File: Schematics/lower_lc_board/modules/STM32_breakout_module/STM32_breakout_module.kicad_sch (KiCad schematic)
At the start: 54 parts, among them J2 SWD_CONN, J3 USB_C_CONN, Q4 2N7002, SW1 SW_STM_RESET, SW2 SW_STM_BOOT_MODE, U5 STM32F103CBT6, U6 W25Q128JVS, U7 ISO1044BDR, U8 CP2102N-Axx-xQFN28, Y1 X322516MMB4SI

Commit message: organizational work
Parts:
- C45: JLCPCB (none) -> C49678
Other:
- moved on the sheet: C22, C45
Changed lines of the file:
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@@
 	)
 	(rectangle
-		(start 104.14 160.02)
-		(end 151.13 185.42)
+		(start 104.394 160.02)
+		(end 144.526 181.356)
 		(stroke
 			(width 0)
@@
 		)
 	)
-	(text "place near PA7 to filter switching noise from adjacent MCO pin "
+	(text "place near PA7 to \nfilter switching noise from \nadjacent MCO pin "
 		(exclude_from_sim no)
-		(at 131.318 179.07 0)
+		(at 154.94 185.166 0)
 		(effects
 			(font
@@
 	(global_label "TEMP_SENSE"
 		(shape input)
-		(at 109.22 170.18 270)
+		(at 149.86 177.8 90)
 		(fields_autoplaced yes)
 		(effects
@@
 		)
 		(property "Intersheetrefs" "${INTERSHEET_REFS}"
-			(at 109.22 185.0183 90)
+			(at 149.86 162.9617 90)
 			(effects
 				(font
@@
 		(lib_name "GND_2")
 		(lib_id "power:GND")
-		(at 116.84 170.18 90)
+		(at 160.02 170.18 180)
 		(unit 1)
 		(exclude_from_sim no)
@@
 		(dnp no)
 		(property "Reference" "#PWR070"
-			(at 123.19 170.18 0)
+			(at 160.02 163.83 0)
 			(effects
 				(font
@@
 		)
 		(property "Value" "GND"
-			(at 120.65 170.1799 90)
+			(at 160.0199 166.37 90)
 			(effects
 				(font
@@
 		)
 		(property "Footprint" ""
-			(at 116.84 170.18 0)
+			(at 160.02 170.18 0)
 			(effects
 				(font
@@
 		)
 		(property "Datasheet" ""
-			(at 116.84 170.18 0)
+			(at 160.02 170.18 0)
 			(effects
 				(font
@@
 		)
 		(property "Description" "Power symbol creates a global label with name \"GND\" , ground"
-			(at 116.84 170.18 0)
+			(at 160.02 170.18 0)
 			(effects
 				(font
@@
 	(symbol
 		(lib_id "Device:C")
-		(at 113.03 170.18 270)
+		(at 160.02 173.99 0)
 		(unit 1)
 		(exclude_from_sim no)
@@
 		(dnp no)
 		(property "Reference" "C45"
-			(at 113.03 164.338 90)
+			(at 154.686 164.338 0)
 			(effects
 				(font
@@
 		)
 		(property "Value" "0.1uF"
-			(at 113.03 166.878 90)
+			(at 154.686 166.878 0)
 			(effects
 				(font
@@
 		)
 		(property "Footprint" "Capacitor_SMD:C_0805_2012Metric"
-			(at 109.22 171.1452 0)
+			(at 160.9852 177.8 0)
 			(effects
 				(font
@@
 		)
 		(property "Datasheet" "~"
-			(at 113.03 170.18 0)
+			(at 160.02 173.99 0)
 			(effects
 				(font
@@
 		)
 		(property "Description" "Unpolarized capacitor"
-			(at 113.03 170.18 0)
+			(at 160.02 173.99 0)
+			(effects
+				(font
+					(size 1.27 1.27)
+				)
+				(hide yes)
+			)
+		)
+		(property "JLCPCB" "C49678"
+			(at 160.02 173.99 0)
 			(effects
 				(font
@@
 	(symbol
 		(lib_id "Device:C")
-		(at 201.93 140.97 90)
+		(at 198.12 147.32 0)
 		(unit 1)
 		(exclude_from_sim no)
@@
 		(on_board yes)
 		(dnp no)
+		(fields_autoplaced yes)
 		(property "Reference" "C22"
-			(at 203.454 135.128 90)
+			(at 201.93 146.0499 0)
 			(effects
 				(font
@@
 		)
 		(property "Value" "0.1uF"
-			(at 204.47 137.16 90)
+			(at 201.93 148.5899 0)
 			(effects
 				(font
@@
 		)
 		(property "Footprint" "Capacitor_SMD:C_0603_1608Metric"
-			(at 205.74 140.0048 0)
+			(at 199.0852 151.13 0)
 			(effects
 				(font
@@
 		)
 		(property "Datasheet" "~"
-			(at 201.93 140.97 0)
+			(at 198.12 147.32 0)
 			(effects
 				(font
@@
 		)
 		(property "Description" "Unpolarized capacitor"
-			(at 201.93 140.97 0)
+			(at 198.12 147.32 0)
 			(effects
 				(font
@@
 	(symbol
 		(lib_id "power:GND")
-		(at 205.74 140.97 0)
+		(at 198.12 151.13 270)
 		(unit 1)
 		(exclude_from_sim no)
@@
 		(dnp no)
 		(property "Reference" "#PWR056"
-			(at 205.74 147.32 0)
+			(at 191.77 151.13 0)
 			(effects
 				(font
@@
 		)
 		(property "Value" "GND"
-			(at 205.74 144.018 90)
+			(at 195.072 151.13 90)
 			(effects
 				(font
@@
 		)
 		(property "Footprint" ""
-			(at 205.74 140.97 0)
+			(at 198.12 151.13 0)
 			(effects
 				(font
@@
 		)
 		(property "Datasheet" ""
-			(at 205.74 140.97 0)
+			(at 198.12 151.13 0)
 			(effects
 				(font
@@
 		)
 		(property "Description" "Power symbol creates a global label with name \"GND\" , ground"
-			(at 205.74 140.97 0)
+			(at 198.12 151.13 0)
 			(effects
 				(font
@@
 	(symbol
 		(lib_id "power:+5V")
-		(at 198.12 140.97 180)
+		(at 198.12 143.51 90)
 		(unit 1)
 		(exclude_from_sim no)
@@
 		(fields_autoplaced yes)
 		(property "Reference" "#PWR053"
-			(at 198.12 137.16 0)
+			(at 201.93 143.51 0)
 			(effects
 				(font
@@
 		)
 		(property "Value" "+5V"
-			(at 198.1199 144.78 90)
+			(at 194.31 143.5099 90)
 			(effects
 				(font
@@
 		)
 		(property "Footprint" ""
-			(at 198.12 140.97 0)
+			(at 198.12 143.51 0)
 			(effects
 				(font
@@
 		)
 		(property "Datasheet" ""
-			(at 198.12 140.97 0)
+			(at 198.12 143.51 0)
 			(effects
 				(font
@@
 		)
 		(property "Description" "Power symbol creates a global label with name \"+5V\""
-			(at 198.12 140.97 0)
+			(at 198.12 143.51 0)
 			(effects
 				(font

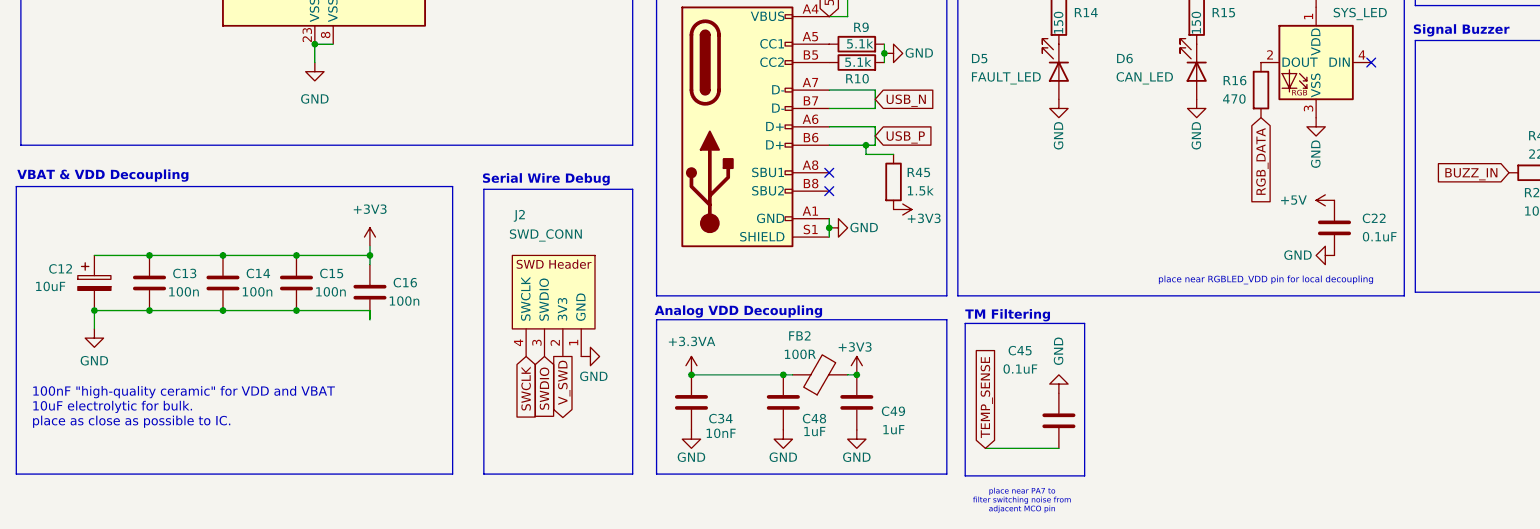
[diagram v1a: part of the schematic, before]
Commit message: more organizational work, add shared footprint, model, symbol dirs and clean up individuals
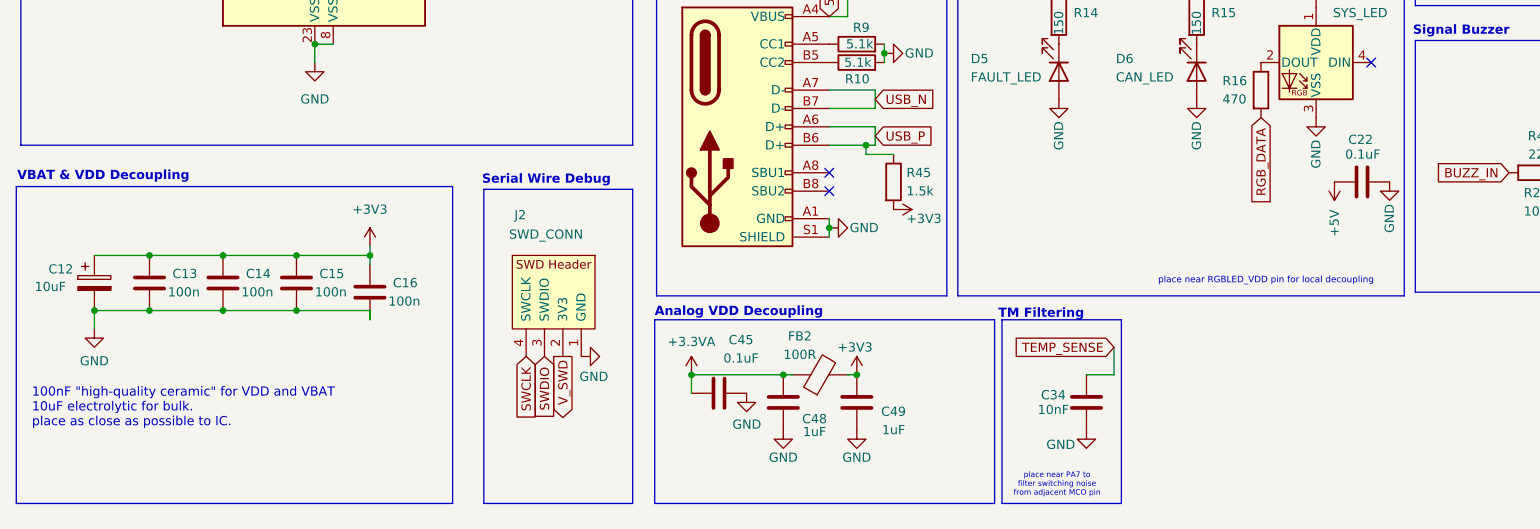
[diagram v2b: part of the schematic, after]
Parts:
- C45: JLCPCB C49678 -> (none)
- FB2: footprint BLM31KN121SN1L:BEADC3216X180N -> Resistor_SMD:R_0805_2012Metric
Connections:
- net +3.3VA: now also C45.2; no longer C34.2
- net TEMP_SENSE: now also C34.2; no longer C45.2
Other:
- title: (none) -> HYDRA | STM32 Breakout Circuitry
- moved on the sheet: C22, C34, C45

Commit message: routing work
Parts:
- removed U8: CP2102N-Axx-xQFN28, Package_DFN_QFN:QFN-28-1EP_5x5mm_P0.5mm_EP3.35x3.35mm, symbol Interface_USB:CP2102N-Axx-xQFN28
- added R48: 10k, Resistor_SMD:R_0402_1005Metric, symbol Device:R
- added U8: CP2102N-Axx-xQFN20, CP2102N_A02_GQFN20:QFN20_CP2102N_SIL, symbol Interface_USB:CP2102N-Axx-xQFN20
- C45: footprint Capacitor_SMD:C_0805_2012Metric -> Capacitor_SMD:C_0603_1608Metric; JLCPCB (none) -> C14663
- C48, C49: footprint Capacitor_SMD:C_0805_2012Metric -> Capacitor_SMD:C_0603_1608Metric; JLCPCB C28323 -> C15849
- R10, R9: footprint Resistor_SMD:R_0603_1608Metric -> Resistor_SMD:R_0402_1005Metric; JLCPCB (none) -> C25905
- R11: footprint Resistor_SMD:R_0603_1608Metric -> Resistor_SMD:R_0402_1005Metric; JLCPCB C31850 -> C25768
- R12: footprint Resistor_SMD:R_0603_1608Metric -> Resistor_SMD:R_0402_1005Metric; JLCPCB C25819 -> C25792
- R13: footprint Resistor_SMD:R_0603_1608Metric -> Capacitor_SMD:C_0402_1005Metric; JLCPCB C21190 -> C11702
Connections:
- net +3V3: now also R48.1, U8.6 (VDD), U8.7 (VREGIN)
- net FL_CS: now also R48.2
- net GND: now also U8.12 (GND), U8.21 (GND), U8.3 (GND)
- net USART_RX: now also U8.18 (TXD)
- net USART_TX: now also U8.17 (RXD)
- net USB_N: now also U8.5 (D-)
- net USB_P: now also U8.4 (D+)
- net at C20.2, R11.1, R12.2: now also U8.8 (VBUS)
- net at R13.1: now also U8.9 (~{RST})
- net ADC_MISO renamed SPI_MISO
- net SPI_MISO: now also U6.2 (DO(IO1))
- net ADC_MOSI renamed SPI_MOSI
- net SPI_MOSI: now also U6.5 (DI(IO0))
- net ADC_SCLK renamed SPI_SCLK
- net SPI_SCLK: now also U6.6 (CLK)
- net FL_MISO: no longer names the net of U5.27 (PB14)
- net FL_MISO: no longer U6.2 (DO(IO1))
- net FL_MOSI: no longer names the net of U5.28 (PB15)
- net FL_MOSI: no longer U6.5 (DI(IO0))
- net FL_SCK: no longer names the net of U5.26 (PB13)
- net FL_SCK: no longer U6.6 (CLK)
- no-connect marks 26 -> 17

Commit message: routing work
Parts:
- R12: now not fitted
- R14, R15: value 150 -> 220; footprint Resistor_SMD:R_0603_1608Metric -> Resistor_SMD:R_0402_1005Metric; JLCPCB (none) -> C25104
- R46: JLCPCB (none) -> C25104
- TP7, TP8: footprint TestPoint:TestPoint_Pad_1.0x1.0mm -> TestPoint:TestPoint_Pad_D1.0mm
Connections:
- net FAULT_LED: now also U5.29 (PA8); no longer U5.30 (PA9)
- net VALVE1_CTRL: now also U5.26 (PB13); no longer U5.31 (PA10)
- net VALVE2_CTRL: now also U5.27 (PB14); no longer U5.29 (PA8)
- new net VSOL-SW: U5.31 (PA10)
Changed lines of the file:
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@@
 		)
 	)
+	(global_label "FAULT_LED"
+		(shape input)
+		(at 74.93 68.58 0)
+		(fields_autoplaced yes)
+		(effects
+			(font
+				(size 1.27 1.27)
+			)
+			(justify left)
+		)
+		(property "Intersheetrefs" "${INTERSHEET_REFS}"
+			(at 87.8333 68.58 0)
+			(effects
+				(font
+					(size 1.27 1.27)
+				)
+				(justify left)
+				(hide yes)
+			)
+		)
+	)
 	(global_label "SWCLK"
 		(shape input)
@@
 		)
 	)
+	(global_label "VSOL-SW"
+		(shape input)
+		(at 74.93 73.66 0)
+		(fields_autoplaced yes)
+		(effects
+			(font
+				(size 1.27 1.27)
+			)
+			(justify left)
+		)
+		(property "Intersheetrefs" "${INTERSHEET_REFS}"
+			(at 86.8052 73.66 0)
+			(effects
+				(font
+					(size 1.27 1.27)
+				)
+				(justify left)
+				(hide yes)
+			)
+		)
+	)
 	(global_label "BOOT0"
 		(shape output)
@@
 		)
 	)
-	(global_label "VALVE1_CTRL"
-		(shape input)
-		(at 74.93 73.66 0)
-		(fields_autoplaced yes)
-		(effects
-			(font
-				(size 1.27 1.27)
-			)
-			(justify left)
-		)
-		(property "Intersheetrefs" "${INTERSHEET_REFS}"
-			(at 90.0709 73.66 0)
-			(effects
-				(font
-					(size 1.27 1.27)
-				)
-				(justify left)
-				(hide yes)
-			)
-		)
-	)
 	(global_label "BUZZ_IN"
 		(shape input)
@@
 		)
 	)
-	(global_label "FAULT_LED"
+	(global_label "VALVE2_CTRL"
 		(shape input)
-		(at 74.93 71.12 0)
+		(at 41.91 111.76 180)
 		(fields_autoplaced yes)
 		(effects
@@
 				(size 1.27 1.27)
 			)
-			(justify left)
+			(justify right)
 		)
 		(property "Intersheetrefs" "${INTERSHEET_REFS}"
-			(at 87.8333 71.12 0)
+			(at 26.7691 111.76 0)
 			(effects
 				(font
 					(size 1.27 1.27)
 				)
-				(justify left)
+				(justify right)
 				(hide yes)
 			)
@@
 		)
 	)
-	(global_label "VALVE2_CTRL"
-		(shape input)
-		(at 74.93 68.58 0)
-		(fields_autoplaced yes)
-		(effects
-			(font
-				(size 1.27 1.27)
-			)
-			(justify left)
-		)
-		(property "Intersheetrefs" "${INTERSHEET_REFS}"
-			(at 90.0709 68.58 0)
-			(effects
-				(font
-					(size 1.27 1.27)
-				)
-				(justify left)
-				(hide yes)
-			)
-		)
-	)
 	(global_label "RESET_FL"
 		(shape output)
@@
 		)
 	)
+	(global_label "VALVE1_CTRL"
+		(shape input)
+		(at 41.91 109.22 180)
+		(fields_autoplaced yes)
+		(effects
+			(font
+				(size 1.27 1.27)
+			)
+			(justify right)
+		)
+		(property "Intersheetrefs" "${INTERSHEET_REFS}"
+			(at 26.7691 109.22 0)
+			(effects
+				(font
+					(size 1.27 1.27)
+				)
+				(justify right)
+				(hide yes)
+			)
+		)
+	)
 	(symbol
 		(lib_id "Device:C_Polarized")
@@
 			)
 		)
+		(property "JLCPCB" "C25104"
+			(at 226.06 139.7 0)
+			(effects
+				(font
+					(size 1.27 1.27)
+				)
+				(hide yes)
+			)
+		)
 		(pin "2"
 		)
@@
 			)
 		)
-		(property "Value" "150"
+		(property "Value" "220"
 			(at 179.07 120.65 90)
 			(effects
@@
 			)
 		)
-		(property "Footprint" "Resistor_SMD:R_0603_1608Metric"
+		(property "Footprint" "Resistor_SMD:R_0402_1005Metric"
 			(at 177.292 118.11 90)
 			(effects
@@
 			)
 		)
+		(property "JLCPCB" "C25104"
+			(at 179.07 118.11 0)
+			(effects
+				(font
+					(size 1.27 1.27)
+				)
+				(hide yes)
+			)
+		)
 		(pin "2"
 		)
@@
 			)
 		)
-		(property "Footprint" "TestPoint:TestPoint_Pad_1.0x1.0mm"
+		(property "Footprint" "TestPoint:TestPoint_Pad_D1.0mm"
 			(at 74.93 81.28 0)
 			(effects
@@
 		(in_bom yes)
 		(on_board yes)
-		(dnp no)
+		(dnp yes)
 		(property "Reference" "R12"
 			(at 210.058 62.3458 0)
@@
 			)
 		)
-		(property "Value" "150"
+		(property "Value" "220"
 			(at 160.02 120.65 90)
 			(effects
@@
 			)
 		)
-		(property "Footprint" "Resistor_SMD:R_0603_1608Metric"
+		(property "Footprint" "Resistor_SMD:R_0402_1005Metric"
 			(at 158.242 118.11 90)
 			(effects
@@
 			)
 		)
+		(property "JLCPCB" "C25104"
+			(at 160.02 118.11 0)
+			(effects
+				(font
+					(size 1.27 1.27)
+				)
+				(hide yes)
+			)
+		)
 		(pin "2"
 		)
@@
 			)
 		)
-		(property "Footprint" "TestPoint:TestPoint_Pad_1.0x1.0mm"
+		(property "Footprint" "TestPoint:TestPoint_Pad_D1.0mm"
 			(at 74.93 83.82 0)
 			(effects

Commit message: routing work
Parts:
- R12: now fitted
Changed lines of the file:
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@@
 		(in_bom yes)
 		(on_board yes)
-		(dnp yes)
+		(dnp no)
 		(property "Reference" "R12"
 			(at 210.058 62.3458 0)

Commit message: more routing work
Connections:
- net CAN_LED: now also U5.19 (PB1); no longer U5.12 (PA2)
- net FL_CS: now also U5.18 (PB0); no longer U5.41 (PB5)
- net RGB_DATA: now also U5.41 (PB5); no longer U5.18 (PB0)
- net VPT-SW: now also U5.12 (PA2); no longer U5.19 (PB1)
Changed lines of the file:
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@@
-		)
-	)
-	(global_label "CAN_LED"
-		(shape input)
-		(at 74.93 53.34 0)
-		(fields_autoplaced yes)
-		(effects
-			(font
-				(size 1.27 1.27)
-			)
-			(justify left)
-		)
-		(property "Intersheetrefs" "${INTERSHEET_REFS}"
-			(at 86.019 53.34 0)
-			(effects
-				(font
-					(size 1.27 1.27)
-				)
-				(justify left)
-				(hide yes)
-			)
 		)
 	)
@@
 		)
 	)
-	(global_label "RGB_DATA"
+	(global_label "FL_CS"
 		(shape input)
 		(at 41.91 76.2 180)
@@
 		)
 		(property "Intersheetrefs" "${INTERSHEET_REFS}"
-			(at 29.7324 76.2 0)
+			(at 33.361 76.2 0)
 			(effects
 				(font
@@
 		)
 	)
+	(global_label "CAN_LED"
+		(shape input)
+		(at 41.91 78.74 180)
+		(fields_autoplaced yes)
+		(effects
+			(font
+				(size 1.27 1.27)
+			)
+			(justify right)
+		)
+		(property "Intersheetrefs" "${INTERSHEET_REFS}"
+			(at 30.821 78.74 0)
+			(effects
+				(font
+					(size 1.27 1.27)
+				)
+				(justify right)
+				(hide yes)
+			)
+		)
+	)
 	(global_label "OSC_IN"
 		(shape input)
@@
 		(property "Intersheetrefs" "${INTERSHEET_REFS}"
 			(at 157.5186 87.63 0)
-			(effects
-				(font
-					(size 1.27 1.27)
-				)
-				(justify right)
-				(hide yes)
-			)
-		)
-	)
-	(global_label "VPT-SW"
-		(shape input)
-		(at 41.91 78.74 180)
-		(fields_autoplaced yes)
-		(effects
-			(font
-				(size 1.27 1.27)
-			)
-			(justify right)
-		)
-		(property "Intersheetrefs" "${INTERSHEET_REFS}"
-			(at 31.3653 78.74 0)
 			(effects
 				(font
@@
 		)
 	)
+	(global_label "VPT-SW"
+		(shape input)
+		(at 74.93 53.34 0)
+		(fields_autoplaced yes)
+		(effects
+			(font
+				(size 1.27 1.27)
+			)
+			(justify left)
+		)
+		(property "Intersheetrefs" "${INTERSHEET_REFS}"
+			(at 85.4747 53.34 0)
+			(effects
+				(font
+					(size 1.27 1.27)
+				)
+				(justify left)
+				(hide yes)
+			)
+		)
+	)
 	(global_label "SWDIO"
 		(shape input)
@@
 		)
 	)
+	(global_label "RGB_DATA"
+		(shape input)
+		(at 41.91 88.9 180)
+		(fields_autoplaced yes)
+		(effects
+			(font
+				(size 1.27 1.27)
+			)
+			(justify right)
+		)
+		(property "Intersheetrefs" "${INTERSHEET_REFS}"
+			(at 29.7324 88.9 0)
+			(effects
+				(font
+					(size 1.27 1.27)
+				)
+				(justify right)
+				(hide yes)
+			)
+		)
+	)
 	(global_label "USB_N"
 		(shape input)
@@
 			(effects
 				(font
-					(size 1.27 1.27)
-				)
-				(justify right)
-				(hide yes)
-			)
-		)
-	)
-	(global_label "FL_CS"
-		(shape input)
-		(at 41.91 88.9 180)
-		(fields_autoplaced yes)
-		(effects
-			(font
-				(size 1.27 1.27)
-			)
-			(justify right)
-		)
-		(property "Intersheetrefs" "${INTERSHEET_REFS}"
-			(at 33.361 88.9 0)
-			(effects
-				(font

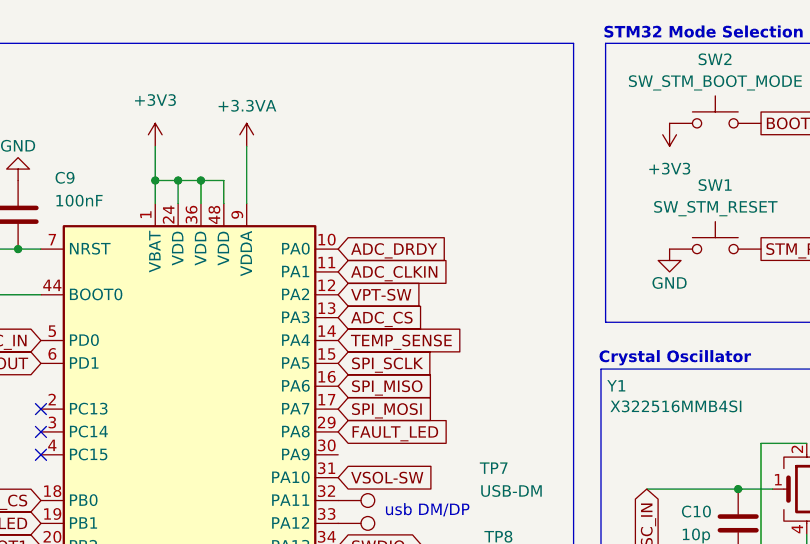
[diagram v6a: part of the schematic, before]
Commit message: ADC routing
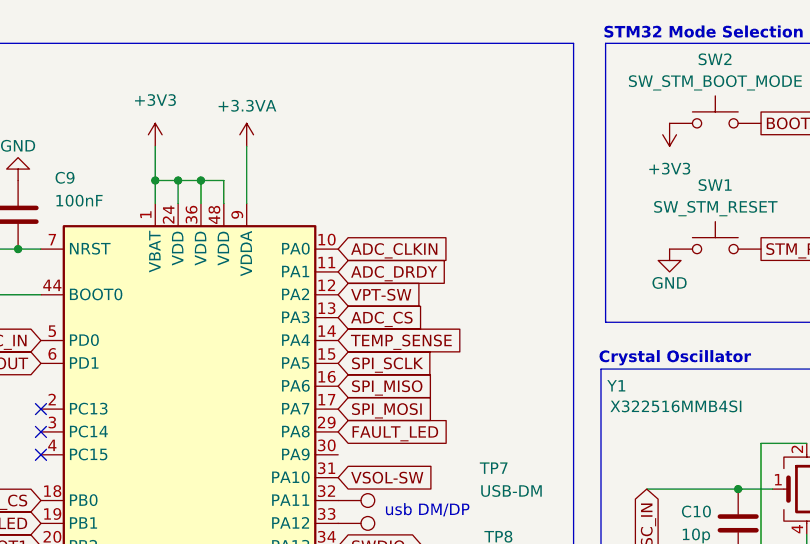
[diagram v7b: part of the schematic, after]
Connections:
- net ADC_CLKIN: now also U5.10 (PA0); no longer U5.11 (PA1)
- net ADC_DRDY: now also U5.11 (PA1); no longer U5.10 (PA0)
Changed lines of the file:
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@@
-		)
-	)
-	(global_label "ADC_DRDY"
-		(shape input)
-		(at 74.93 48.26 0)
-		(fields_autoplaced yes)
-		(effects
-			(font
-				(size 1.27 1.27)
-			)
-			(justify left)
-		)
-		(property "Intersheetrefs" "${INTERSHEET_REFS}"
-			(at 87.41 48.26 0)
-			(effects
-				(font
-					(size 1.27 1.27)
-				)
-				(justify left)
-				(hide yes)
-			)
 		)
 	)
@@
 		)
 	)
-	(global_label "ADC_CLKIN"
-		(shape input)
-		(at 74.93 50.8 0)
-		(fields_autoplaced yes)
-		(effects
-			(font
-				(size 1.27 1.27)
-			)
-			(justify left)
-		)
-		(property "Intersheetrefs" "${INTERSHEET_REFS}"
-			(at 88.0148 50.8 0)
-			(effects
-				(font
-					(size 1.27 1.27)
-				)
-				(justify left)
-				(hide yes)
-			)
-		)
-	)
 	(global_label "FL_CS"
 		(shape input)
@@
 		)
 	)
+	(global_label "ADC_DRDY"
+		(shape input)
+		(at 74.93 50.8 0)
+		(fields_autoplaced yes)
+		(effects
+			(font
+				(size 1.27 1.27)
+			)
+			(justify left)
+		)
+		(property "Intersheetrefs" "${INTERSHEET_REFS}"
+			(at 87.41 50.8 0)
+			(effects
+				(font
+					(size 1.27 1.27)
+				)
+				(justify left)
+				(hide yes)
+			)
+		)
+	)
 	(global_label "VALVE2_CTRL"
 		(shape input)
@@
 				(hide yes)
 			)
+		)
+	)
+	(global_label "ADC_CLKIN"
+		(shape input)
+		(at 74.93 48.26 0)
+		(fields_autoplaced yes)
+		(effects
+			(font
+				(size 1.27 1.27)
+			)
+			(justify left)
+		)
+		(property "Intersheetrefs" "${INTERSHEET_REFS}"
+			(at 88.0148 48.26 0)
+			(effects
+				(font
+					(size 1.27 1.27)
+				)
+				(justify left)
+				(hide yes)
+			)

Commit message: routing work
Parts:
- C34: footprint Capacitor_SMD:C_0603_1608Metric -> Capacitor_SMD:C_0402_1005Metric
- R7, R8: footprint Resistor_SMD:R_0603_1608Metric -> Resistor_SMD:R_0402_1005Metric; JLCPCB C25804 -> C25744
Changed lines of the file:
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@@
 			)
 		)
-		(property "Footprint" "Capacitor_SMD:C_0603_1608Metric"
+		(property "Footprint" "Capacitor_SMD:C_0402_1005Metric"
 			(at 162.8648 167.64 0)
 			(effects
@@
 			)
 		)
-		(property "Footprint" "Resistor_SMD:R_0603_1608Metric"
+		(property "Footprint" "Resistor_SMD:R_0402_1005Metric"
 			(at 159.258 46.99 90)
 			(effects
@@
 			)
 		)
-		(property "JLCPCB" "C25804"
+		(property "JLCPCB" "C25744"
 			(at 157.48 46.99 0)
 			(effects
@@
 			)
 		)
-		(property "Footprint" "Resistor_SMD:R_0603_1608Metric"
+		(property "Footprint" "Resistor_SMD:R_0402_1005Metric"
 			(at 151.638 46.99 90)
 			(effects
@@
 			)
 		)
-		(property "JLCPCB" "C25804"
+		(property "JLCPCB" "C25744"
 			(at 149.86 46.99 0)
 			(effects
